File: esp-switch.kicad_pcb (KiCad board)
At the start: 2 copper layers, 50.8 x 50.8 mm, 28 parts, among them J1 Screw_Terminal_01x03, J2 Conn_01x04, J4 Conn_01x04, J5 Screw_Terminal_01x02, U1 ATTINY441-SSU, U2 ESP-01v090, U3 MOC3041M, U4 MOC3041M, U5 HLK-PM05

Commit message: V2 - traced all the channels from RF
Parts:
- U5: value HLK-PM05 -> HLK-PM03
- moved U1 0.64 mm to (188.6, 134.0)
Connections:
- net +5V renamed +3V3
- RF1 pad 5: Net-(RF1-Pad4) -> Net-(RF1-Pad5)
- RF1 pad 6: Net-(RF1-Pad3) -> Net-(RF1-Pad6)
- U1 pad 10: Net-(RF1-Pad4) -> Net-(RF1-Pad3)
- U1 pad 11: Net-(U1-Pad11) -> Net-(RF1-Pad4)
- U1 pad 12: Net-(U1-Pad12) -> Net-(RF1-Pad5)
- U1 pad 13: Net-(RF1-Pad3) -> Net-(RF1-Pad6)
- U2 pad 1: Net-(U1-Pad11) -> Net-(J2-Pad1)
- U2 pad 4: Net-(J2-Pad1) -> Net-(J2-Pad3)
- U2 pad 8: Net-(U1-Pad12) -> Net-(J2-Pad2)
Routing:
- net Net-(J2-Pad3): track 18.9 -> 48.0 mm
- net Net-(RF1-Pad6): track 0.00 -> 26.9 mm
- net Net-(RF1-Pad5): track 0.00 -> 22.5 mm
- net Net-(J2-Pad2): track 23.6 -> 43.2 mm, vias 1 -> 2
- net Net-(J2-Pad1): track 51.7 -> 36.3 mm, vias 2 -> 1
- net Net-(U1-Pad11): track 14.2 -> 0.00 mm
- net Net-(U1-Pad12): track 13.9 -> 0.00 mm
- net Net-(RF1-Pad3): track 32.1 -> 18.4 mm
- net Net-(D2-Pad2): track 51.5 -> 53.6 mm
- net Net-(D1-Pad2): track 45.6 -> 47.7 mm
- net GND: track 111.9 -> 110.5 mm
- net Net-(RF1-Pad4): track 20.1 -> 19.3 mm
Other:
- board text added: "© 2018 Foxel V2"
- board text removed: "© 2018 Foxel"

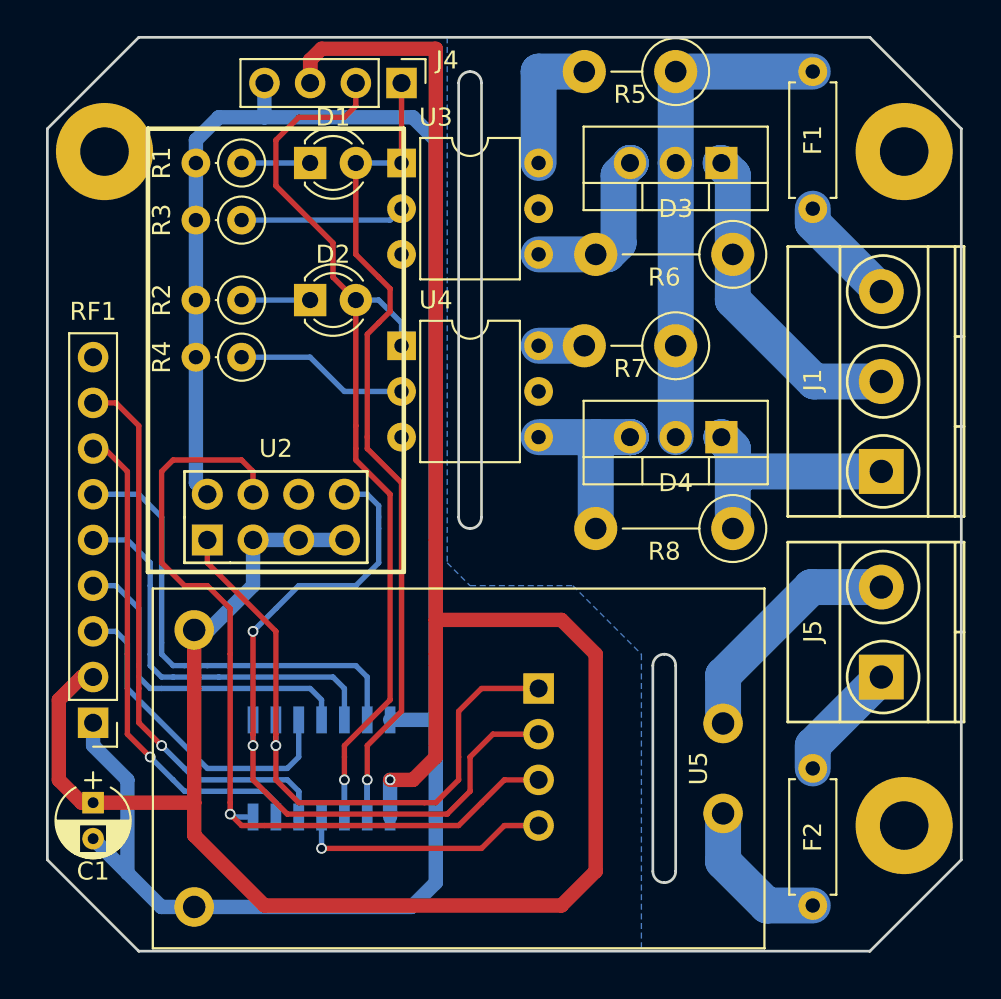
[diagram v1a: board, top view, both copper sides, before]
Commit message: V3: mains with shared L and multiple N terminals programming interface for ATTINY moved so can be soldered ATTINY reset available from ESP GPIO0
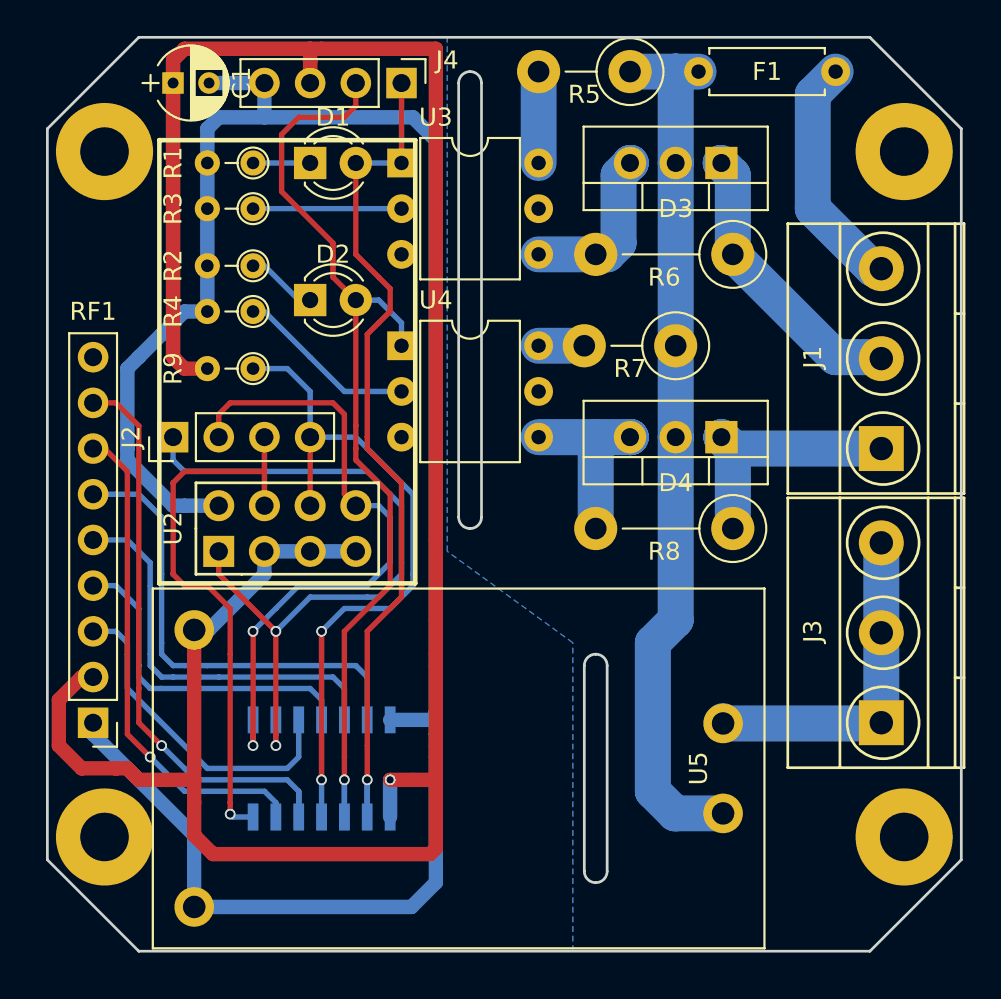
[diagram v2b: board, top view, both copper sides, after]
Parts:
- removed F2: Fuse_Small, Resistors_THT:R_Axial_DIN0207_L6.3mm_D2.5mm_P7.62mm_Horizontal
- removed J5: Screw_Terminal_01x02, Connectors_Terminal_Blocks:TerminalBlock_Pheonix_MKDS1.5-2pol
- added J3: Screw_Terminal_01x03, Connectors_Terminal_Blocks:TerminalBlock_Pheonix_MKDS1.5-3pol, F.Cu at (219.7, 131.4)
- added R9: 10K, Resistors_THT:R_Axial_DIN0204_L3.6mm_D1.6mm_P2.54mm_Vertical, F.Cu at (184.8, 111.8)
- added REF**: MountingHole_2.7mm_M2.5_Pad, Mounting_Holes:MountingHole_2.7mm_M2.5_Pad, F.Cu at (176.5, 137.8)
- J2: moved to F.Cu
- R1, R2, R3, R4: footprint Resistors_THT:R_Axial_DIN0207_L6.3mm_D2.5mm_P2.54mm_Vertical -> Resistors_THT:R_Axial_DIN0204_L3.6mm_D1.6mm_P2.54mm_Vertical
- moved C1 40.3 mm to (180.3, 95.9), turned to 0 degrees
- moved J2 24.7 mm to (180.3, 115.6), turned to 90 degrees
- moved F1 6.35 mm to (209.6, 95.2), turned to 0 degrees
- moved R4 2.62 mm to (184.8, 108.6)
- moved R5 2.54 mm to (205.7, 95.2)
- moved R2 2.01 mm to (184.8, 106.0)
- moved J1 1.27 mm to (219.7, 116.2)
- moved U2 0.90 mm to (182.9, 121.9)
- moved R3 0.90 mm to (184.8, 102.9)
- moved R1 0.63 mm to (184.8, 100.3)
- moved REF** 0.63 mm to (221.0, 137.8)
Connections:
- U2 pad 6: (no net) -> Net-(J2-Pad4)
- U5 pad 1: Net-(F2-Pad1) -> Net-(D3-Pad2)
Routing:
- net Net-(J2-Pad4): track 15.0 -> 38.6 mm, vias 1 -> 2
- net Net-(D3-Pad2): track 27.9 -> 48.8 mm
- net Net-(J2-Pad3): track 48.0 -> 31.0 mm
- net Net-(F2-Pad1): track 8.73 -> 0.00 mm
- net Net-(J2-Pad2): track 43.2 -> 35.8 mm
- net Net-(F1-Pad2): track 6.18 -> 13.3 mm
- net Net-(F2-Pad2): track 6.66 -> 0.00 mm
- net GND: track 110.5 -> 116.1 mm
- net Net-(J3-Pad1): track 13.6 -> 19.1 mm
- net Net-(J2-Pad1): track 36.3 -> 40.7 mm, vias 1 -> 2
- net +3V3: track 138.4 -> 135.4 mm
- net Net-(R5-Pad2): track 7.62 -> 5.08 mm
- net Net-(D3-Pad1): track 18.1 -> 16.0 mm
- net Net-(R3-Pad1): track 9.15 -> 8.25 mm
- net Net-(D4-Pad1): track 14.8 -> 15.4 mm
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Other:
- outline, holes or cut-outs redrawn
- board text added: "© 2018 Foxel V3"
- board text removed: "© 2018 Foxel V2"

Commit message: V4 schematics
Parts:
- removed D1, D2: LED, LEDs:LED_D3.0mm
- removed J4: Conn_01x04, Pin_Headers:Pin_Header_Straight_1x04_Pitch2.54mm
- removed R1, R2: 470R, Resistors_THT:R_Axial_DIN0204_L3.6mm_D1.6mm_P2.54mm_Vertical
- D3, D4: value BT137 -> BTA08-600BW
- J1, J3: value Screw_Terminal_01x03 -> Screw_Terminal_01x02; footprint Connectors_Terminal_Blocks:TerminalBlock_Pheonix_MKDS1.5-3pol -> Connectors_Terminal_Blocks:TerminalBlock_Pheonix_MKDS1.5-2pol
- R3, R4: value 470R -> 150R
- U3, U4: value MOC3041M -> MOC3043M
- moved F1 39.9 mm to (215.9, 134.6), turned to 90 degrees
- moved J2 24.0 mm to (199.4, 130.2), turned to 0 degrees
- moved C1 12.1 mm to (180.3, 108.0)
- moved J3 11.9 mm to (214.6, 120.7)
- moved J1 7.65 mm to (214.6, 110.5)
- moved REF** 5.99 mm to (215.9, 141.0)
- moved D3 5.99 mm to (205.7, 103.5)
- moved R6 5.68 mm to (206.4, 108.0)
- moved D4 5.43 mm to (205.7, 117.5)
- moved R8 5.24 mm to (206.4, 121.9)
- moved R7 5.12 mm to (203.8, 113.0)
- moved REF** 5.12 mm to (215.9, 100.3)
- moved U3 5.08 mm to (188.0, 100.3)
- moved U4 5.08 mm to (188.0, 110.5)
- moved R4 4.45 mm to (184.8, 113.0)
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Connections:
- J3 pad 1: Net-(J3-Pad1) -> Net-(F1-Pad2)
- J3 pad 2: Net-(J3-Pad1) -> Net-(J3-Pad2)
- U5 pad 2: Net-(J3-Pad1) -> Net-(J3-Pad2)
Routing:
- net +3V3: track 135.4 -> 96.5 mm
- net Net-(J2-Pad3): track 31.0 -> 56.9 mm, vias 1 -> 2
- net GND: track 116.1 -> 93.9 mm
- net Net-(J4-Pad2): track 53.3 -> 33.2 mm, vias 1 -> 2
- net Net-(J3-Pad1): track 19.1 -> 0.00 mm
- net Net-(J3-Pad2): track 0.00 -> 18.7 mm
- net Net-(J2-Pad1): track 40.7 -> 28.5 mm
- net Net-(J2-Pad4): track 38.6 -> 46.5 mm
- net Net-(R4-Pad1): track 10.1 -> 3.18 mm
- net Net-(F1-Pad2): track 13.3 -> 6.88 mm
- net Net-(J4-Pad1): track 47.7 -> 42.3 mm, vias 1 -> 2
- net Net-(R3-Pad1): track 8.25 -> 3.18 mm
- net Net-(J2-Pad2): track 35.8 -> 40.8 mm
- net Net-(D2-Pad1): track 3.96 -> 0.00 mm
- net Net-(D1-Pad1): track 3.18 -> 0.00 mm
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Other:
- board size 50.8 x 50.8 mm -> 45.7 x 47 mm
- board text added: "L"
- board text added: "L1"
- board text added: "L2"
- board text added: "N"
- board text added: "© 2020 Foxel V4"
- board text removed: "© 2018 Foxel V3"

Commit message: V4 smaller PCB
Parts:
- removed R8: 470R, Resistors_THT:R_Axial_DIN0411_L9.9mm_D3.6mm_P7.62mm_Vertical
- removed the REF** at (215.9, 100.3)
- removed the REF** at (176.5, 141.0)
- removed the REF** at (176.5, 100.3)
- added R4: 390R, Resistors_THT:R_Axial_DIN0207_L6.3mm_D2.5mm_P5.08mm_Vertical, F.Cu at (203.8, 100.3)
- J3: renamed from J2; moved to B.Cu
- R5, R7: value 390R -> 470R; footprint Resistors_THT:R_Axial_DIN0411_L9.9mm_D3.6mm_P5.08mm_Vertical -> Resistors_THT:R_Axial_DIN0207_L6.3mm_D2.5mm_P5.08mm_Vertical
- R6: value 470R -> 390R; footprint Resistors_THT:R_Axial_DIN0411_L9.9mm_D3.6mm_P7.62mm_Vertical -> Resistors_THT:R_Axial_DIN0207_L6.3mm_D2.5mm_P5.08mm_Vertical
- moved REF** 27.4 mm to (196.8, 121.3)
- moved R5 9.86 mm to (206.4, 108.6)
- moved R7 8.64 mm to (206.4, 121.3)
- moved R6 5.12 mm to (203.8, 112.4)
- moved RF1 2.54 mm to (175.9, 134.0)
- moved D2 1.42 mm to (206.4, 116.2)
- moved D1 0.90 mm to (206.4, 104.1)
- turned J3 to 180 degrees
- renumbered D3 to D1, D4 to D2, J3 to J1, J1 to J2, R9 to R1, R3 to R2, R4 to R3
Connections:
- D1 pad 1: Net-(D3-Pad1) -> Net-(D1-Pad1)
- D1 pad 2: Net-(D3-Pad2) -> Net-(D1-Pad2)
- D1 pad 3: Net-(D3-Pad3) -> Net-(D1-Pad3)
- D2 pad 1: Net-(D4-Pad1) -> Net-(D2-Pad1)
- D2 pad 2: Net-(D3-Pad2) -> Net-(D1-Pad2)
- D2 pad 3: Net-(D4-Pad3) -> Net-(D2-Pad3)
- F1 pad 1: Net-(D3-Pad2) -> Net-(D1-Pad2)
- J2 pad 1: Net-(D4-Pad1) -> Net-(D2-Pad1)
- J2 pad 2: Net-(D3-Pad1) -> Net-(D1-Pad1)
- R5 pad 1: Net-(D3-Pad2) -> Net-(D1-Pad1)
- R5 pad 2: Net-(R5-Pad2) -> Net-(D1-Pad3)
- R6 pad 1: Net-(D3-Pad1) -> Net-(D1-Pad2)
- R6 pad 2: Net-(D3-Pad3) -> Net-(R6-Pad2)
- R7 pad 1: Net-(D3-Pad2) -> Net-(D2-Pad1)
- R7 pad 2: Net-(R7-Pad2) -> Net-(D2-Pad3)
- U3 pad 4: Net-(D3-Pad3) -> Net-(D1-Pad3)
- U3 pad 6: Net-(R5-Pad2) -> Net-(R4-Pad2)
- U4 pad 4: Net-(D4-Pad3) -> Net-(D2-Pad3)
- U4 pad 6: Net-(R7-Pad2) -> Net-(R6-Pad2)
- U5 pad 1: Net-(D3-Pad2) -> Net-(D1-Pad2)
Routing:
- net Net-(D3-Pad2): track 50.1 -> 0.00 mm
- net Net-(D1-Pad2): track 0.00 -> 46.2 mm
- net Net-(D4-Pad1): track 18.1 -> 0.00 mm
- net Net-(D2-Pad1): track 0.00 -> 15.7 mm
- net Net-(D1-Pad1): track 0.00 -> 13.3 mm
- net Net-(D3-Pad1): track 13.0 -> 0.00 mm
- net Net-(D2-Pad3): track 0.00 -> 11.1 mm
- net Net-(D1-Pad3): track 0.00 -> 10.9 mm
- net Net-(D4-Pad3): track 10.3 -> 0.00 mm
- net Net-(D3-Pad3): track 8.41 -> 0.00 mm
- net Net-(R7-Pad2): track 4.60 -> 0.00 mm
- net Net-(R6-Pad2): track 0.00 -> 3.96 mm
- net Net-(R5-Pad2): track 3.70 -> 0.00 mm
- net Net-(R4-Pad2): track 0.00 -> 3.17 mm
- net Net-(RF1-Pad6): track 26.9 -> 24.1 mm
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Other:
- board size 45.7 x 47 mm -> 45.7 x 45.7 mm
- board text added: "ISP"
- board text added: "S1"
- board text added: "S2"
- board text added: "S3"
- board text added: "S4"
- board text added: "© 2020 Foxel V3s"
- board text removed: "© 2020 Foxel V4"
